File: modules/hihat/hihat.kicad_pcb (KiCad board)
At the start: 2 copper layers, 30.5 x 68.6 mm, 52 parts, among them U1 VTL5C, U2 MCP6002-xSN, U3 MCP6002-xSN, U4 MCP6002-xSN, U5 ATtiny1616-M

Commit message: hihat: Renamed U and TX silkscreen text
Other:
- board text added: "HIHAT 0.3.0"
- board text removed: "HIHAT 0.2.0"
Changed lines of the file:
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@@
 		)
 	)
-	(gr_text "HIHAT\n0.2.0"
+	(gr_text "HIHAT\n0.3.0"
 		(at 76.327 107.95 0)
 		(layer "F.SilkS")
@@
 		)
 	)
-	(gr_text "U"
-		(at 66.802 99.441 0)
+	(gr_text "TX"
+		(at 66.04 99.441 0)
 		(layer "F.SilkS")
 		(effects
@@
 		)
 	)
-	(gr_text "TX"
-		(at 64.008 99.441 0)
+	(gr_text "U"
+		(at 63.754 99.441 0)
 		(layer "F.SilkS")
 		(effects

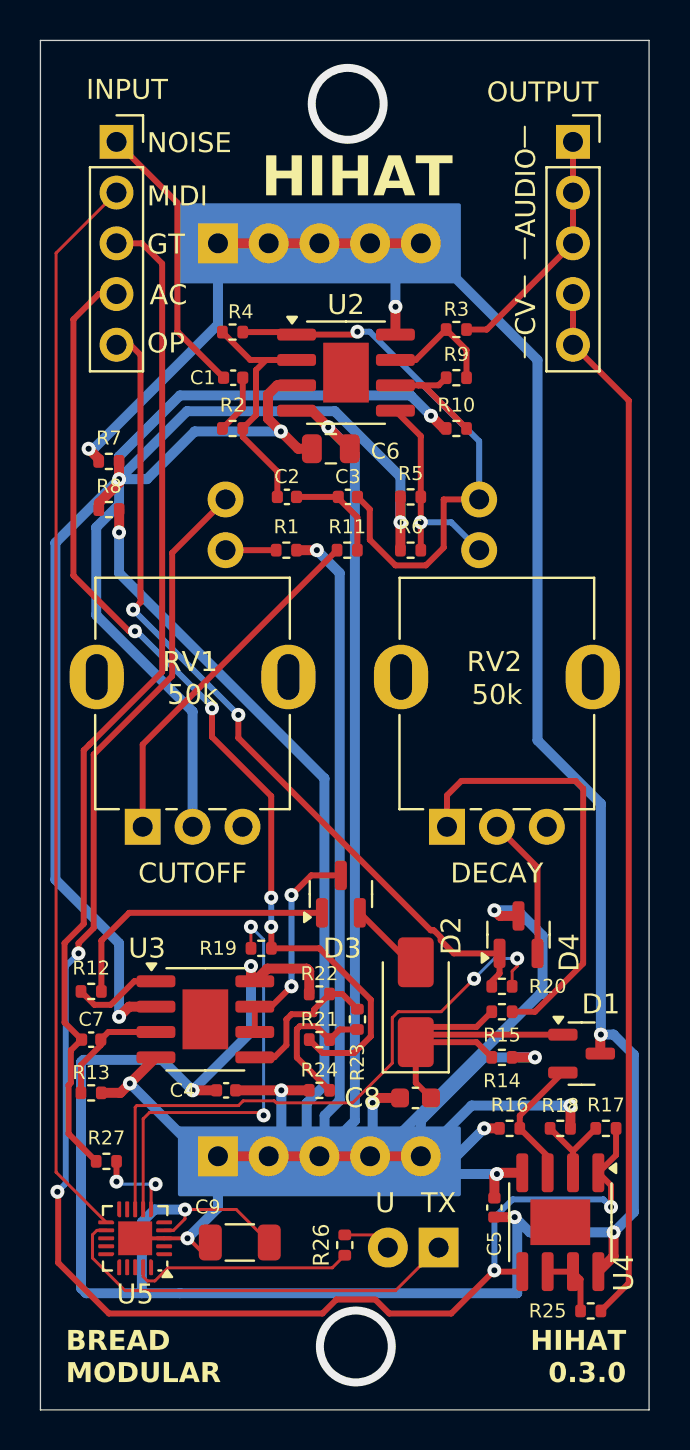
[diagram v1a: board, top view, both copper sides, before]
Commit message: hihat: Add MIDI THRU support
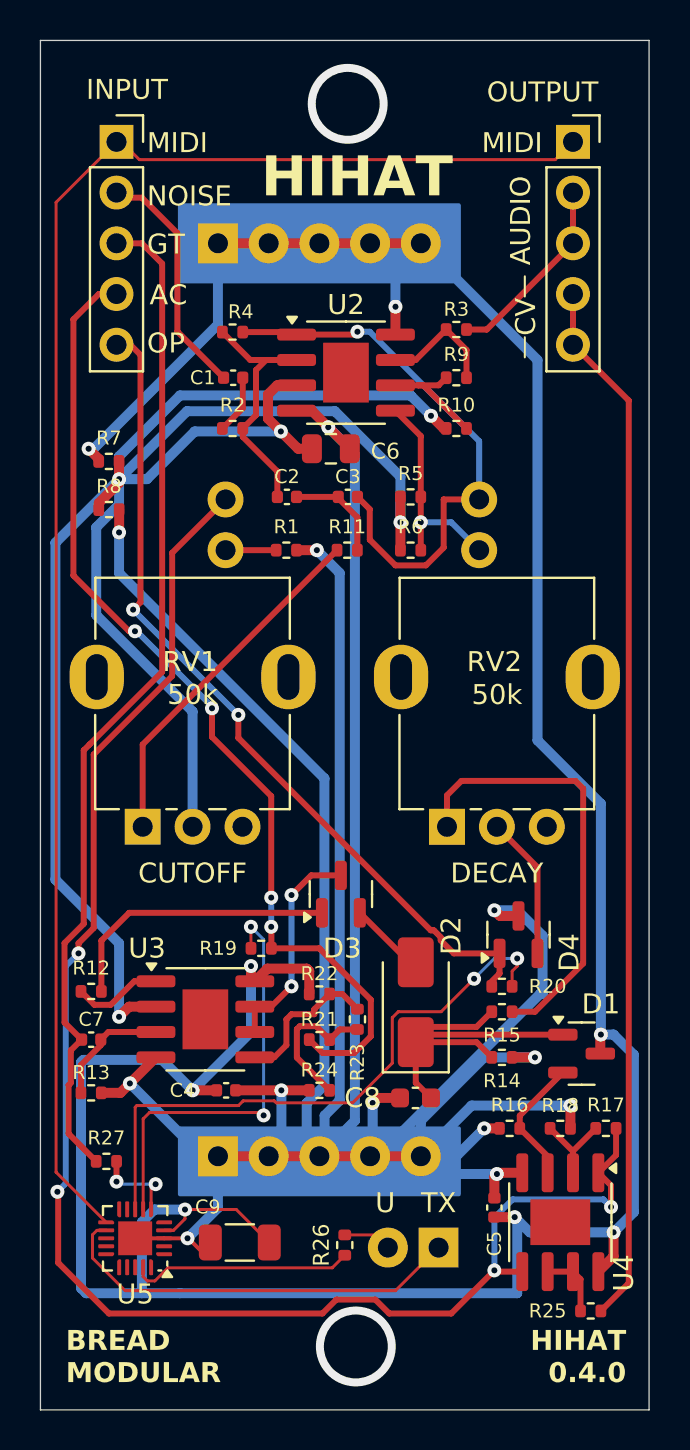
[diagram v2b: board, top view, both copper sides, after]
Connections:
- INPUT1 pad 1: NOISE_IN -> MIDI
- INPUT1 pad 2: MIDI -> NOISE_IN
- OUTPUT1 pad 1: HIHAT_OUT -> MIDI
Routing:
- net MIDI: track 53.9 -> 80.0 mm
- net HIHAT_OUT: track 12.2 -> 9.66 mm
- net NOISE_IN: track 14.0 -> 11.7 mm
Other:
- board text added: "HIHAT 0.4.0"
- board text removed: "HIHAT 0.3.0"
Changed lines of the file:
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@@
 			(layers "*.Cu" "*.Mask")
 			(remove_unused_layers no)
-			(net 2 "NOISE_IN")
+			(net 6 "MIDI")
 			(pinfunction "Pin_1")
 			(pintype "passive")
@@
 			(layers "*.Cu" "*.Mask")
 			(remove_unused_layers no)
-			(net 6 "MIDI")
+			(net 2 "NOISE_IN")
 			(pinfunction "Pin_2")
 			(pintype "passive")
@@
 			(layers "*.Cu" "*.Mask")
 			(remove_unused_layers no)
-			(net 20 "HIHAT_OUT")
+			(net 6 "MIDI")
 			(pinfunction "Pin_1")
 			(pintype "passive")
@@
 	)
 	(gr_line
-		(start 71.247 51.562)
-		(end 71.247 50.546)
-		(stroke
-			(width 0.1)
-			(type default)
-		)
-		(layer "F.SilkS")
-	)
-	(gr_line
-		(start 71.247 45.974)
-		(end 71.247 44.958)
-		(stroke
-			(width 0.1)
-			(type default)
-		)
-		(layer "F.SilkS")
-	)
-	(gr_line
 		(start 46.99 109.22)
 		(end 77.47 109.22)
@@
 	)
 	(gr_text "MIDI"
+		(at 72.136 46.355 0)
+		(layer "F.SilkS")
+		(effects
+			(font
+				(size 1 1)
+				(thickness 0.15)
+			)
+			(justify right bottom)
+		)
+	)
+	(gr_text "NOISE"
 		(at 52.324 49.022 0)
 		(layer "F.SilkS")
@@
 	)
 	(gr_text "AUDIO"
-		(at 71.882 48.26 90)
+		(at 71.628 49.657 90)
 		(layer "F.SilkS")
 		(effects
@@
 		)
 	)
-	(gr_text "HIHAT\n0.3.0"
+	(gr_text "HIHAT\n0.4.0"
 		(at 76.327 107.95 0)
 		(layer "F.SilkS")
@@
 		)
 	)
-	(gr_text "NOISE"
+	(gr_text "MIDI"
 		(at 52.324 46.355 0)
 		(layer "F.SilkS")
@@
 	)
 	(segment
+		(start 53.848 50.292)
+		(end 52.07 48.514)
+		(width 0.3)
+		(layer "F.Cu")
+		(net 2)
+	)
+	(segment
 		(start 53.848 55.217)
-		(end 56.162 57.531)
+		(end 53.848 50.292)
 		(width 0.3)
 		(layer "F.Cu")
@@
 	)
 	(segment
-		(start 53.848 48.768)
+		(start 51.14704 48.514)
+		(end 51.10052 48.56052)
+		(width 0.3)
+		(layer "F.Cu")
+		(net 2)
+	)
+	(segment
+		(start 56.162 57.531)
 		(end 53.848 55.217)
 		(width 0.3)
@@
 	)
 	(segment
-		(start 50.8 45.72)
-		(end 53.848 48.768)
+		(start 52.07 48.514)
+		(end 51.14704 48.514)
 		(width 0.3)
 		(layer "F.Cu")
@@
 	)
 	(segment
+		(start 50.8 45.72)
+		(end 51.17 46.09)
+		(width 0.15)
+		(layer "F.Cu")
+		(net 6)
+	)
+	(segment
+		(start 47.771975 48.748025)
+		(end 50.8 45.72)
+		(width 0.15)
+		(layer "F.Cu")
+		(net 6)
+	)
+	(segment
+		(start 72.771 46.609)
+		(end 73.66 45.72)
+		(width 0.15)
+		(layer "F.Cu")
+		(net 6)
+	)
+	(segment
+		(start 51.943 46.609)
+		(end 72.771 46.609)
+		(width 0.15)
+		(layer "F.Cu")
+		(net 6)
+	)
+	(segment
+		(start 51.17 46.09)
+		(end 51.424 46.09)
+		(width 0.15)
+		(layer "F.Cu")
+		(net 6)
+	)
+	(segment
 		(start 50.283 99.828)
 		(end 47.771975 97.316975)
@@
 	)
 	(segment
-		(start 47.771975 97.316975)
-		(end 47.771975 51.288025)
+		(start 51.424 46.09)
+		(end 51.943 46.609)
 		(width 0.15)
 		(layer "F.Cu")
@@
 	)
 	(segment
-		(start 47.771975 51.288025)
-		(end 50.8 48.26)
+		(start 47.771975 97.316975)
+		(end 47.771975 48.748025)
 		(width 0.15)
 		(layer "F.Cu")
@@
 	)
 	(segment
-		(start 73.66 45.72)
-		(end 73.66 50.8)
+		(start 73.66 50.8)
+		(end 73.66 48.26)
 		(width 0.3)
 		(layer "F.Cu")

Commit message: hihat_1.0.0
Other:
- board text added: "HIHAT 1.0.0"
- board text removed: "HIHAT 0.4.0"
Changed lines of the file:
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@@
 		)
 	)
-	(gr_text "HIHAT\n0.4.0"
+	(gr_text "HIHAT\n1.0.0"
 		(at 76.327 107.95 0)
 		(layer "F.SilkS")
